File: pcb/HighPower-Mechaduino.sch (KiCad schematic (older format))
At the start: 50 parts, among them J1 SUPPLY, J2 STEPPER, P1 SWD, P4 -, P5 -, P6 -, P7 -, Q1 SSM3J328R, Q2 BSS138, SW1 SW_PUSH, U1 AS5047D, U2 AP2112K-3.3TRG1, U3 AT24CS64-SSHM

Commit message: Add oval mounting holes to support NEMA23 as well as NEMA24
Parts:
- P4, P5, P6, P7: footprint Mounting_Holes:MountingHole_4.3mm_M4_Pad_Via -> Mounting_Holes_local:MountingHole_4.3x6.2mm_M4_Pad_Via
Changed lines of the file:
@@
 	3800 1300 3800 1500
 Wire Wire Line
-	3700 1200 3700 1300
-Wire Wire Line
-	3700 1300 3700 1500
+	3700 1200 3700 1500
 Wire Wire Line
 	3700 1300 3600 1300
@@
 	8700 2300 8800 2300
 Wire Wire Line
-	8700 800  8700 1000
-Wire Wire Line
-	8700 1000 8700 2300
+	8700 800  8700 2300
 Wire Wire Line
 	8700 1000 8800 1000
@@
 	8600 3000 8800 3000
 Wire Wire Line
-	8600 1700 8600 2300
-Wire Wire Line
-	8600 2300 8600 3000
+	8600 1700 8600 3000
 Wire Wire Line
 	8600 1700 8800 1700
@@
 $EndComp
 Wire Wire Line
-	7750 2800 7950 2800
-Wire Wire Line
-	7950 2800 8250 2800
-Wire Wire Line
-	8250 2800 8800 2800
+	7750 2800 8800 2800
 Wire Wire Line
 	7450 1500 7050 1500
@@
 	1200 4650 1200 5050
 Wire Wire Line
-	1200 4450 1150 4450
-Wire Wire Line
-	1150 4450 1100 4450
-Wire Wire Line
-	1700 4450 1800 4450
-Wire Wire Line
-	1800 4450 2300 4450
-Wire Wire Line
-	2300 4450 2750 4450
-Wire Wire Line
-	1800 4100 1800 4450
-Wire Wire Line
-	1800 4450 1800 4600
+	1100 4450 1200 4450
+Wire Wire Line
+	1700 4450 2750 4450
+Wire Wire Line
+	1800 4100 1800 4600
 Wire Wire Line
 	1800 4900 1800 5050
@@
 $EndComp
 Wire Wire Line
-	2750 4350 2750 4450
-Wire Wire Line
-	2750 4450 2750 4600
+	2750 4350 2750 4600
 Connection ~ 1800 4450
 Wire Wire Line
@@
 $EndComp
 Wire Wire Line
-	3650 6700 3650 6800
-Wire Wire Line
-	3650 6800 3650 6950
-Wire Wire Line
-	3650 6950 3650 7050
+	3650 6700 3650 7050
 $Comp
 L GND #PWR017
@@
 	4700 6800 4850 6800
 Wire Wire Line
-	4850 6700 4850 6800
-Wire Wire Line
-	4850 6800 4850 7050
+	4850 6700 4850 7050
 Wire Wire Line
 	4850 7350 4850 7450
@@
 	900  1700 800  1700
 Wire Wire Line
-	800  1700 800  1800
-Wire Wire Line
-	800  1800 800  1900
-Wire Wire Line
-	800  1900 800  2000
-Wire Wire Line
-	800  2000 800  2100
+	800  1700 800  2100
 Wire Wire Line
 	800  2000 900  2000
@@
 	2300 1550 2300 1450
 Wire Wire Line
-	2300 1850 2300 2000
-Wire Wire Line
-	2300 2000 2300 2100
+	2300 1850 2300 2100
 $Comp
 L GND #PWR024
@@
 $EndComp
 Wire Wire Line
-	5250 2500 5500 2500
-Wire Wire Line
-	5500 2500 5600 2500
+	5250 2500 5600 2500
 Wire Wire Line
 	5500 2500 5500 2600
@@
 	1000 6000 800  6000
 Wire Wire Line
-	800  5900 800  6000
-Wire Wire Line
-	800  6000 800  6100
-Wire Wire Line
-	800  6100 800  6200
+	800  5900 800  6200
 Wire Wire Line
 	800  6100 1000 6100
@@
 	2450 6000 2600 6000
 Wire Wire Line
-	2600 5900 2600 6000
-Wire Wire Line
-	2600 6000 2600 6350
+	2600 5900 2600 6350
 Connection ~ 2600 6000
 $Comp
@@
 	800  7000 800  6900
 Wire Wire Line
-	800  6500 800  6550
-Wire Wire Line
-	800  6550 800  6600
+	800  6500 800  6600
 Connection ~ 800  6100
 Wire Wire Line
@@
 	5900 6900 5800 6900
 Wire Wire Line
-	5800 6900 5800 7000
-Wire Wire Line
-	5800 7000 5800 7100
-Wire Wire Line
-	5800 7100 5800 7250
-Wire Wire Line
-	5800 7250 5800 7550
+	5800 6900 5800 7550
 Wire Wire Line
 	5900 7000 5800 7000
@@
 $EndComp
 Wire Wire Line
-	7750 1500 7950 1500
-Wire Wire Line
-	7950 1500 8250 1500
-Wire Wire Line
-	8250 1500 8800 1500
+	7750 1500 8800 1500
 Wire Wire Line
 	8250 1600 8250 1500
@@
 F 0 "P4" V 3465 4862 50  0000 R CNN
 F 1 "-" V 3374 4862 50  0000 R CNN
-F 2 "Mounting_Holes:MountingHole_4.3mm_M4_Pad_Via" H 3500 4950 50  0001 C CNN
+F 2 "Mounting_Holes_local:MountingHole_4.3x6.2mm_M4_Pad_Via" H 3500 4950 50  0001 C CNN
 F 3 "" H 3500 4950 50  0000 C CNN
 	1    3500 4950
@@
 F 0 "P5" V 3665 4862 50  0000 R CNN
 F 1 "-" V 3574 4862 50  0000 R CNN
-F 2 "Mounting_Holes:MountingHole_4.3mm_M4_Pad_Via" H 3700 4950 50  0001 C CNN
+F 2 "Mounting_Holes_local:MountingHole_4.3x6.2mm_M4_Pad_Via" H 3700 4950 50  0001 C CNN
 F 3 "" H 3700 4950 50  0000 C CNN
 	1    3700 4950
@@
 F 0 "P6" V 3865 4862 50  0000 R CNN
 F 1 "-" V 3774 4862 50  0000 R CNN
-F 2 "Mounting_Holes:MountingHole_4.3mm_M4_Pad_Via" H 3900 4950 50  0001 C CNN
+F 2 "Mounting_Holes_local:MountingHole_4.3x6.2mm_M4_Pad_Via" H 3900 4950 50  0001 C CNN
 F 3 "" H 3900 4950 50  0000 C CNN
 	1    3900 4950
@@
 F 0 "P7" V 4065 4862 50  0000 R CNN
 F 1 "-" V 3974 4862 50  0000 R CNN
-F 2 "Mounting_Holes:MountingHole_4.3mm_M4_Pad_Via" H 4100 4950 50  0001 C CNN
+F 2 "Mounting_Holes_local:MountingHole_4.3x6.2mm_M4_Pad_Via" H 4100 4950 50  0001 C CNN
 F 3 "" H 4100 4950 50  0000 C CNN
 	1    4100 4950

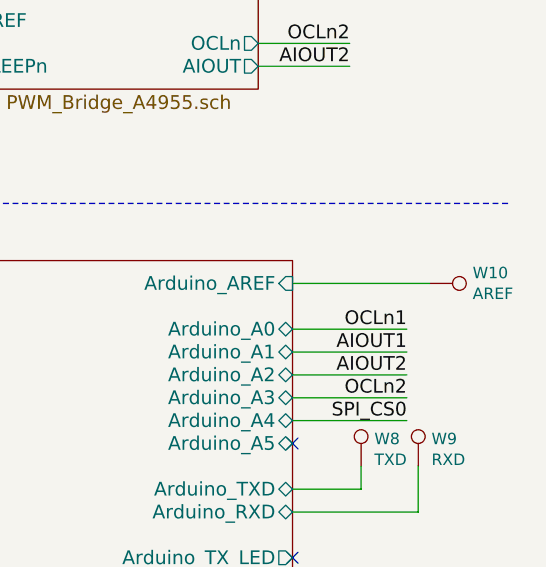
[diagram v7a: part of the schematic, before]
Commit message: Move processor part a bit down
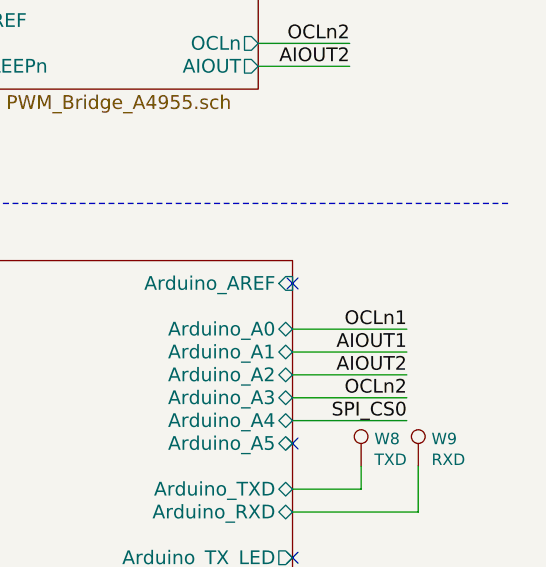
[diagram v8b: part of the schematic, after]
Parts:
- removed W10: AREF, Measurement_Points:Measurement_Point_Round-SMD-Pad_Small, symbol TEST_1P
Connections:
- no-connect marks 16 -> 17
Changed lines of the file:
@@
 	10800 4950 10800 4750
-$Comp
-L TEST_1P W10
-U 1 1 581727E3
-P 10850 3950
-F 0 "W10" V 10804 4138 50  0000 L CNN
-F 1 "AREF" V 10895 4138 50  0000 L CNN
-F 2 "Measurement_Points:Measurement_Point_Round-SMD-Pad_Small" H 11050 3950 50  0001 C CNN
-F 3 "" H 11050 3950 50  0000 C CNN
-	1    10850 3950
-	0    1    1    0
-$EndComp
-Wire Wire Line
-	10250 3950 10850 3950
 $Comp
 L TEST_1P W5
@@
 Wire Wire Line
 	6050 5750 6050 5900
+NoConn ~ 10250 3950
 $EndSCHEMATC
